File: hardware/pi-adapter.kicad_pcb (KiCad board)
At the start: 2 copper layers, 64 x 56 mm, 37 parts, among them P1 CONN_02X20, P10 CONN_01X04, P100 CONN_01X01, P101 CONN_01X01, P103 CONN_01X01, P11 CONN_01X04, P12 CONN_01X04, P13 CONN_01X04, P14 CONN_01X04, P15 CONN_01X04, P16 CONN_01X04, P17 CONN_01X04, P18 CONN_01X04, P19 CONN_01X04, P2 +5V, P20 CONN_01X04, P21 CONN_01X04, P22 CONN_01X06, P3 CONN_01X03, P4 GND, P5 CONN_01X03, P6 CONN_01X04, P7 CONN_01X04, P8 CONN_01X04, P9 CONN_01X04, U1 74HCT245, U2 74HCT245, U3 74HCT245, U4 74HCT245

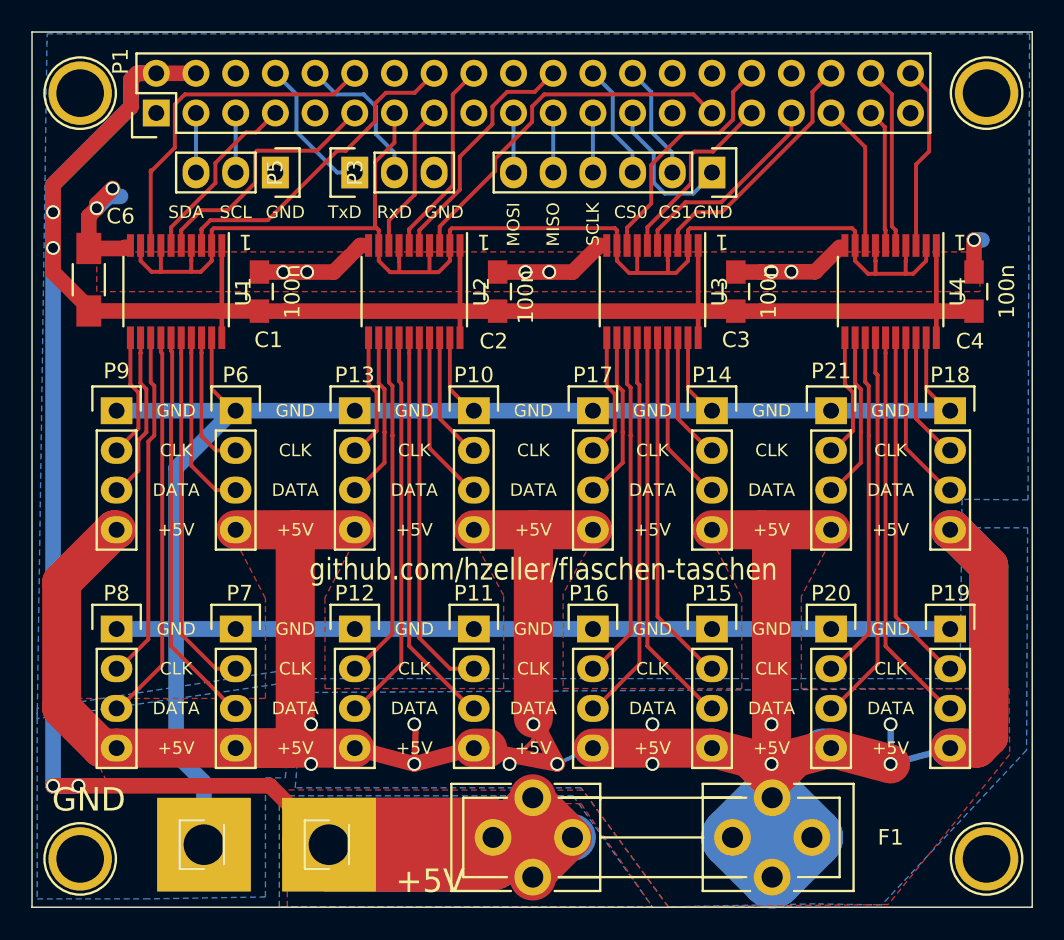
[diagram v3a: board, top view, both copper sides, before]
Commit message: o Add thermal reliefs for GND. o Add rounded corners.
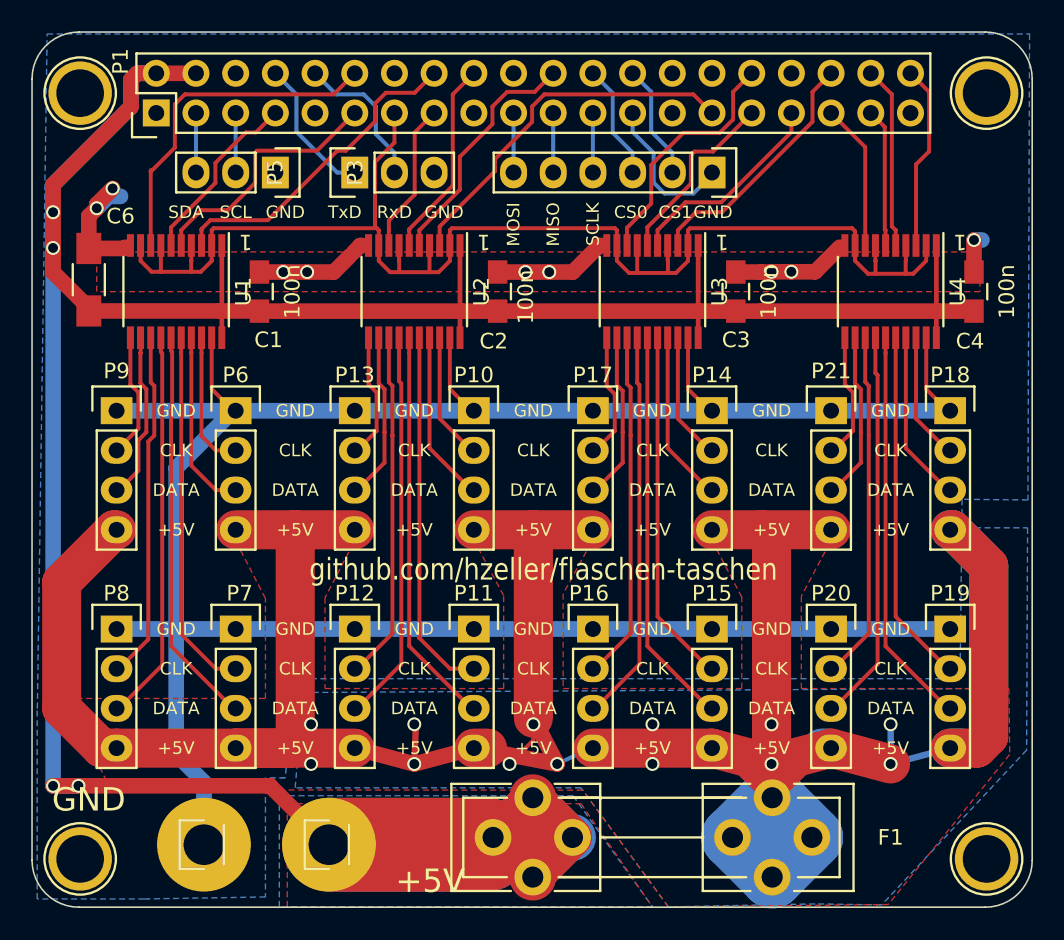
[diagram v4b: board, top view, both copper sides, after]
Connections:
- P1 pad 9: GND -> (no net)
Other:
- outline, holes or cut-outs redrawn
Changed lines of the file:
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@@
-(kicad_pcb (version 4) (host pcbnew "(2015-08-05 BZR 6054, Git 5c8efeb)-product")
+(kicad_pcb (version 4) (host pcbnew "(2016-02-20 BZR 6576, Git d7e2ffe)-product")
   (general
-    (links 151)
-    (no_connects 1)
+    (links 150)
+    (no_connects 0)
     (area 97.971667 37.949999 166.188334 96.86)
     (thickness 1.6)
-    (drawings 80)
+    (drawings 84)
     (tracks 574)
     (zones 0)
@@
       (hpglpenspeed 20)
       (hpglpendiameter 15)
-      (hpglpenoverlay 2)
       (psnegative false)
       (psa4output false)
@@
     (pad 8 thru_hole oval (at 2.54 7.62 90) (size 1.7272 1.7272) (drill 1.016) (layers *.Cu *.Mask F.SilkS)
       (net 61 "Net-(P1-Pad8)"))
-    (pad 9 thru_hole oval (at 0 10.16 90) (size 1.7272 1.7272) (drill 1.016) (layers *.Cu *.Mask F.SilkS)
-      (net 2 GND))
+    (pad 9 thru_hole oval (at 0 10.16 90) (size 1.7272 1.7272) (drill 1.016) (layers *.Cu *.Mask F.SilkS))
     (pad 10 thru_hole oval (at 2.54 10.16 90) (size 1.7272 1.7272) (drill 1.016) (layers *.Cu *.Mask F.SilkS)
       (net 4 "Net-(P1-Pad10)"))
@@
     (fp_line (start -1.55 -1.55) (end 1.55 -1.55) (layer F.SilkS) (width 0.15))
     (fp_line (start -1.27 1.27) (end 1.27 1.27) (layer F.SilkS) (width 0.15))
-    (pad 1 thru_hole rect (at 0 0 90) (size 6 6) (drill 2.6) (layers *.Cu *.Mask F.SilkS)
+    (pad 1 thru_hole oval (at 0 0 90) (size 6 6) (drill 2.6) (layers *.Cu *.Mask F.SilkS)
       (net 1 VCC))
   )
@@
     (fp_line (start -1.55 -1.55) (end 1.55 -1.55) (layer F.SilkS) (width 0.15))
     (fp_line (start -1.27 1.27) (end 1.27 1.27) (layer F.SilkS) (width 0.15))
-    (pad 1 thru_hole rect (at 0 0 90) (size 6 6) (drill 2.6) (layers *.Cu *.Mask F.SilkS)
+    (pad 1 thru_hole circle (at 0 0 90) (size 6 6) (drill 2.6) (layers *.Cu *.Mask F.SilkS)
       (net 2 GND))
   )
@@
     )
   )
+  (gr_arc (start 103 91) (end 103 94) (angle 90) (layer Edge.Cuts) (width 0.1))
+  (gr_arc (start 161 91) (end 164 91) (angle 90) (layer Edge.Cuts) (width 0.1))
+  (gr_arc (start 161 41) (end 161 38) (angle 90) (layer Edge.Cuts) (width 0.1))
+  (gr_arc (start 103 41) (end 100 41) (angle 90) (layer Edge.Cuts) (width 0.1))
   (gr_text CLK (at 139.7 64.77) (layer F.SilkS)
     (effects (font (size 0.8 0.8) (thickness 0.15)))
@@
     (effects (font (size 1.4 1.2) (thickness 0.2)))
   )
-  (gr_line (start 100 94) (end 100 38) (angle 90) (layer Edge.Cuts) (width 0.1))
-  (gr_line (start 100 38) (end 164 38) (angle 90) (layer Edge.Cuts) (width 0.1))
-  (gr_line (start 164 38) (end 164 94) (angle 90) (layer Edge.Cuts) (width 0.1))
-  (gr_line (start 164 94) (end 100 94) (angle 90) (layer Edge.Cuts) (width 0.1))
+  (gr_line (start 100 91) (end 100 41) (angle 90) (layer Edge.Cuts) (width 0.1))
+  (gr_line (start 103 38) (end 161 38) (angle 90) (layer Edge.Cuts) (width 0.1))
+  (gr_line (start 164 41) (end 164 91) (angle 90) (layer Edge.Cuts) (width 0.1))
+  (gr_line (start 161 94) (end 103 94) (angle 90) (layer Edge.Cuts) (width 0.1))
   (segment (start 134.5819 89.535) (end 129.5019 89.535) (width 3) (layer B.Cu) (net 1))
   (segment (start 132.0419 86.995) (end 132.0419 92.075) (width 3) (layer F.Cu) (net 1))
@@
   )
   (zone (net 2) (net_name GND) (layer B.Cu) (hatch edge 0.508)
-    (connect_pads yes (clearance 0.508))
+    (connect_pads (clearance 0.508))
     (min_thickness 0.254)
-    (fill yes (arc_segments 16) (thermal_gap 0.508) (thermal_bridge_width 0.508) (smoothing fillet) (radius 0.5))
+    (fill yes (arc_segments 16) (thermal_gap 0.508) (thermal_bridge_width 1.8))
     (polygon
       (pts
-        (xy 100.965 38.119407) (xy 163.83 38.119407) (xy 163.7284 67.939007) (xy 159.512 67.900907) (xy 159.385 79.375)
-        (xy 118.11 79.375) (xy 100.33 81.934407)
-      )
-    )
-  )
-  (zone (net 2) (net_name GND) (layer B.Cu) (hatch edge 0.508)
-    (connect_pads yes (clearance 0.508))
-    (min_thickness 0.254)
-    (fill yes (arc_segments 16) (thermal_gap 0.508) (thermal_bridge_width 0.508) (smoothing fillet) (radius 0.5))
-    (polygon
-      (pts
-        (xy 107.188 93.472) (xy 114.935 93.345) (xy 114.935 85.725) (xy 116.205 85.725) (xy 116.84 78.74)
-        (xy 100.33 81.28) (xy 100.33 93.472)
+        (xy 163.7284 67.939007) (xy 159.512 67.900907) (xy 159.385 79.375) (xy 118.11 79.375) (xy 116.764667 79.568659)
+        (xy 116.205 85.725) (xy 114.935 85.725) (xy 114.935 93.345) (xy 107.188 93.472) (xy 100.33 93.472)
+        (xy 100.33 81.28) (xy 100.339505 81.278538) (xy 100.965 38.119407) (xy 163.83 38.119407) (xy 163.7284 67.939007)
       )
     )
@@
     (connect_pads yes (clearance 0.508))
     (min_thickness 0.254)
-    (fill yes (arc_segments 16) (thermal_gap 0.508) (thermal_bridge_width 0.508) (smoothing fillet) (radius 0.5))
+    (fill yes (arc_segments 16) (thermal_gap 0.508) (thermal_bridge_width 1.8) (smoothing fillet) (radius 0.5))
     (polygon
       (pts
@@
     (connect_pads yes (clearance 0.508))
     (min_thickness 0.254)
-    (fill yes (arc_segments 16) (thermal_gap 0.508) (thermal_bridge_width 0.508) (smoothing fillet) (radius 0.5))
+    (fill yes (arc_segments 16) (thermal_gap 0.508) (thermal_bridge_width 1.8) (smoothing fillet) (radius 0.5))
     (polygon
       (pts

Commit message: o Rename header references for easier connecting.
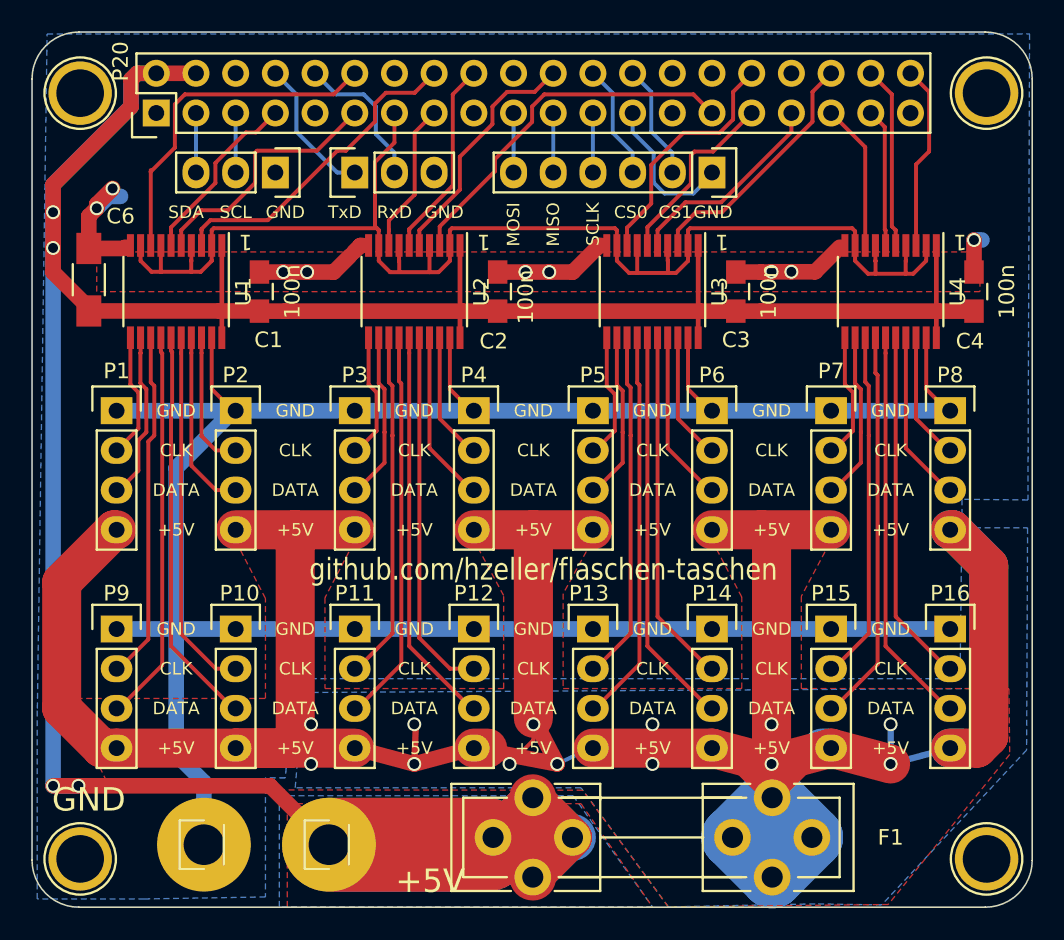
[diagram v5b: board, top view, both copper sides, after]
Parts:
- renumbered P9 to P1, P7 to P10, P12 to P11, P11 to P12, P16 to P13, P15 to P14, P20 to P15, P19 to P16, P6 to P2, P1 to P20, P3 to P21, P5 to P23, P13 to P3, P10 to P4, P100 to P40, P101 to P41, P103 to P43, P17 to P5, P14 to P6, P21 to P7, P18 to P8, P8 to P9

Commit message: o Some more renaming needed.
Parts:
- renumbered P2 to P30, P4 to P31
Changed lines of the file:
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@@
     (links 150)
     (no_connects 0)
-    (area 97.971667 37.949999 166.188334 96.86)
+    (area 99.949999 37.949999 164.050001 94.050001)
     (thickness 1.6)
     (drawings 84)
@@
     (descr "Through hole pin header")
     (tags "pin header")
-    (fp_text reference P2 (at -2.286 0 180) (layer F.SilkS) hide
+    (fp_text reference P30 (at -2.286 0 180) (layer F.SilkS) hide
       (effects (font (size 1 1) (thickness 0.15)))
     )
@@
     (descr "Through hole pin header")
     (tags "pin header")
-    (fp_text reference P4 (at 0.254 2.54 90) (layer F.SilkS) hide
-      (effects (font (size 1 1) (thickness 0.15)))
-    )
+    (fp_text reference P31 (at 0.254 2.54 90) (layer F.SilkS) hide
+      (effects (font (size 1 1) (thickness 0.15)))
+    )
